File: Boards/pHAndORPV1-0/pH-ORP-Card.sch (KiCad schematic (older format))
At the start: 110 parts, among them IC1 PIC32MM0064GPM028, P1 ICSP, P2 AquaPicBus, P3 Power, P4 pH, P5 pH/ORP, Q1 NX7002AK, Q2 NX7002AK, Q3 NX7002AK, Q4 AO3407A, U1 AP2114H, U10 LTC2483, U11 Si8602, U12 TC7660, U2 ST485EC, U3 LMC6061, U4 TLV272, U5 LTC2483, U6 Si8602, U7 TC7660, U8 LMC6061, U9 TLV272, X1 8MHz

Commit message: worked on pH ORP board layout
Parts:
- P4, P5: footprint A_MyFootPrints:BNC_Socket_TYCO-AMP_LargePads -> MyFootPrints:BNC_Socket_TYCO-AMP_LargePads
- PS1, PS2: footprint A_MyFootPrints:8-SMD -> MyFootPrints:8-SMD
- RV1, RV2, RV3, RV4: footprint A_MyFootPrints:POTENTIAMETER_SMD -> MyFootPrints:POTENTIAMETER_SMD
- U10, U5: footprint A_MyFootPrints:DFN-10_3x3mm -> MyFootPrints:DFN-10_3x3mm
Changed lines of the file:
@@
 F 0 "P4" H 1660 1320 60  0000 C CNN
 F 1 "pH" V 1760 1140 40  0000 C CNN
-F 2 "A_MyFootPrints:BNC_Socket_TYCO-AMP_LargePads" H 1650 1200 60  0001 C CNN
+F 2 "MyFootPrints:BNC_Socket_TYCO-AMP_LargePads" H 1650 1200 60  0001 C CNN
 F 3 "~" H 1650 1200 60  0000 C CNN
 	1    1650 1200
@@
 F 0 "RV2" V 5150 2600 50  0000 C CNN
 F 1 "10K" V 5250 2600 50  0000 C CNN
-F 2 "A_MyFootPrints:POTENTIAMETER_SMD" H 5250 2600 60  0001 C CNN
+F 2 "MyFootPrints:POTENTIAMETER_SMD" H 5250 2600 60  0001 C CNN
 F 3 "~" H 5250 2600 60  0000 C CNN
 	1    5250 2600
@@
 F 0 "RV1" V 2850 2200 40  0000 C CNN
 F 1 "50K" V 2950 2200 40  0000 C CNN
-F 2 "A_MyFootPrints:POTENTIAMETER_SMD" H 2950 2200 60  0001 C CNN
+F 2 "MyFootPrints:POTENTIAMETER_SMD" H 2950 2200 60  0001 C CNN
 F 3 "~" H 2950 2200 60  0000 C CNN
 	1    2950 2200
@@
 F 0 "PS2" H 11250 4900 60  0000 C CNN
 F 1 "R1SE-0505" H 11450 4100 60  0000 C CNN
-F 2 "A_MyFootPrints:8-SMD" H 11450 4500 60  0001 C CNN
+F 2 "MyFootPrints:8-SMD" H 11450 4500 60  0001 C CNN
 F 3 "~" H 11450 4500 60  0000 C CNN
 	1    11450 4500
@@
 F 0 "PS1" H 11250 2000 60  0000 C CNN
 F 1 "R1SE-0505" H 11450 1200 60  0000 C CNN
-F 2 "A_MyFootPrints:8-SMD" H 11450 1600 60  0001 C CNN
+F 2 "MyFootPrints:8-SMD" H 11450 1600 60  0001 C CNN
 F 3 "~" H 11450 1600 60  0000 C CNN
 	1    11450 1600
@@
 F 0 "U5" H 7200 2500 60  0000 C CNN
 F 1 "LTC2483" H 7100 1900 60  0000 C CNN
-F 2 "A_MyFootPrints:DFN-10_3x3mm" H 7700 2200 60  0001 C CNN
+F 2 "MyFootPrints:DFN-10_3x3mm" H 7700 2200 60  0001 C CNN
 F 3 "~" H 7700 2200 60  0000 C CNN
 	1    7700 2200
@@
 F 0 "U10" H 7200 5400 60  0000 C CNN
 F 1 "LTC2483" H 7100 4800 60  0000 C CNN
-F 2 "A_MyFootPrints:DFN-10_3x3mm" H 7700 5100 60  0001 C CNN
+F 2 "MyFootPrints:DFN-10_3x3mm" H 7700 5100 60  0001 C CNN
 F 3 "~" H 7700 5100 60  0000 C CNN
 	1    7700 5100
@@
 F 0 "RV4" V 5150 5500 50  0000 C CNN
 F 1 "10K" V 5250 5500 50  0000 C CNN
-F 2 "A_MyFootPrints:POTENTIAMETER_SMD" H 5250 5500 60  0001 C CNN
+F 2 "MyFootPrints:POTENTIAMETER_SMD" H 5250 5500 60  0001 C CNN
 F 3 "~" H 5250 5500 60  0000 C CNN
 	1    5250 5500
@@
 F 0 "RV3" V 2850 5100 40  0000 C CNN
 F 1 "50K" V 2950 5100 40  0000 C CNN
-F 2 "A_MyFootPrints:POTENTIAMETER_SMD" H 2950 5100 60  0001 C CNN
+F 2 "MyFootPrints:POTENTIAMETER_SMD" H 2950 5100 60  0001 C CNN
 F 3 "~" H 2950 5100 60  0000 C CNN
 	1    2950 5100
@@
 F 0 "P5" H 1660 4220 60  0000 C CNN
 F 1 "pH/ORP" V 1760 4040 40  0000 C CNN
-F 2 "A_MyFootPrints:BNC_Socket_TYCO-AMP_LargePads" H 1650 4100 60  0001 C CNN
+F 2 "MyFootPrints:BNC_Socket_TYCO-AMP_LargePads" H 1650 4100 60  0001 C CNN
 F 3 "~" H 1650 4100 60  0000 C CNN
 	1    1650 4100

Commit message: added firmware for the pH ORP Card
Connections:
- net LED_R: now also IC1.3 (RB2); no longer IC1.1 (RB0)
- net LED_Y: now also IC1.1 (RB0); no longer IC1.3 (RB2)
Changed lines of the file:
@@
 RX_LV
 Text Label 2900 7400 2    60   ~ 0
-LED_Y
+LED_R
 Text Label 2900 7300 2    60   ~ 0
 LED_G
 Text Label 2900 7200 2    60   ~ 0
-LED_R
+LED_Y
 $Comp
 L TRI-LED D1

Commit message: something changed in schematic
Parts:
- D1: value SMP4-RGY -> SMTL4-RGY
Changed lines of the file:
@@
 P 3950 7250
 F 0 "D1" H 3950 7600 50  0000 C CNN
-F 1 "SMP4-RGY" H 3950 6860 50  0000 C CNN
+F 1 "SMTL4-RGY" H 3950 6860 50  0000 C CNN
 F 2 "MyFootPrints:PLCC-4" H 3950 7500 60  0001 C CNN
 F 3 "~" H 3950 7500 60  0000 C CNN

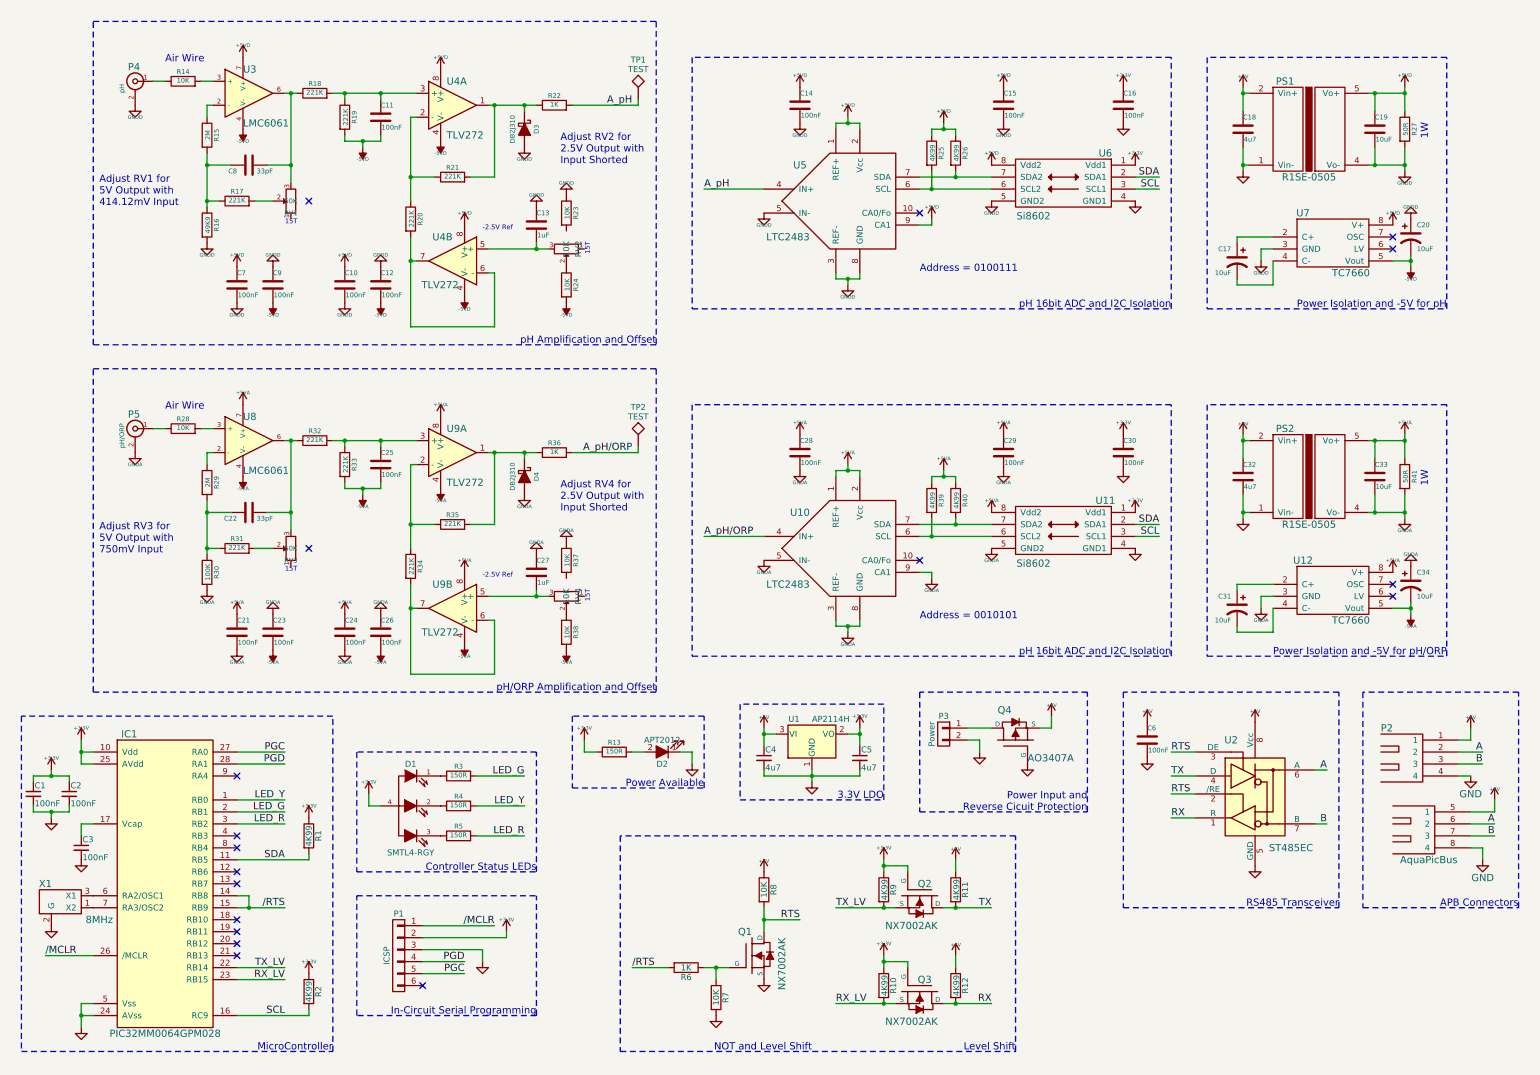
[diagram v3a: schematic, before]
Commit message: added enable disable for ph isolation
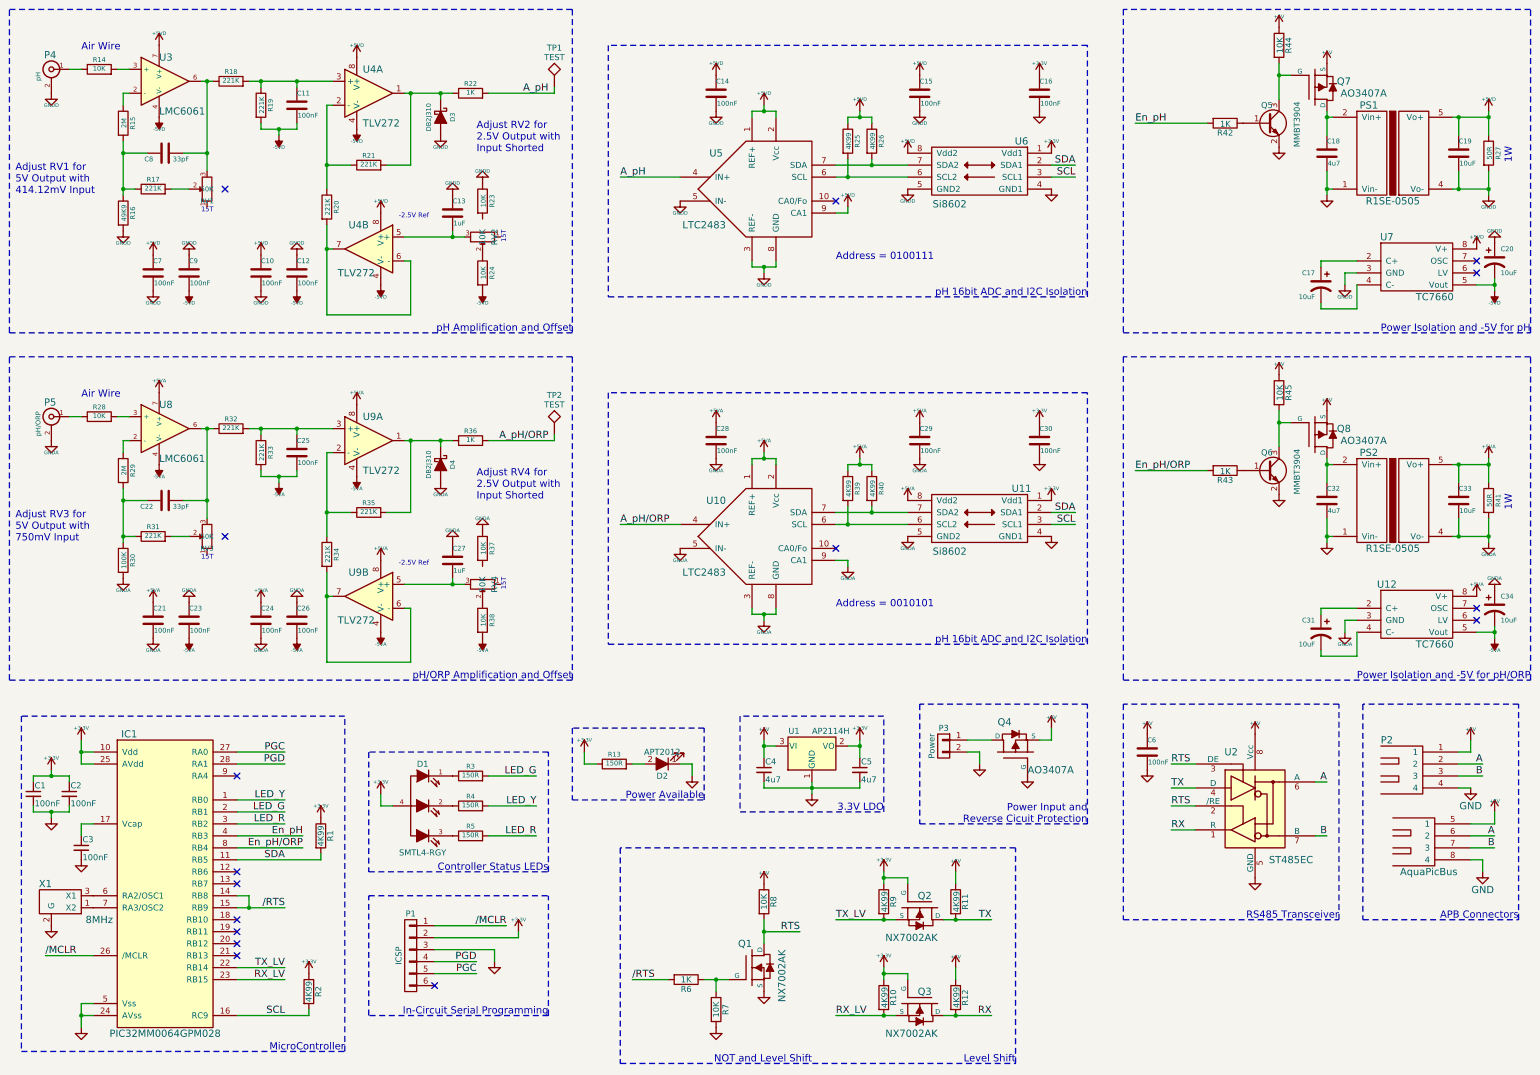
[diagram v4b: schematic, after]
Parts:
- added Q5, Q6: MMBT3904, TO_SOT_Packages_SMD:SOT-23, symbol Q_NPN_BEC
- added Q7, Q8: AO3407A, TO_SOT_Packages_SMD:SOT-23, symbol MOSFET_P_SMALL
- added R42, R43: 1K, Resistors_SMD:R_0805, symbol R
- added R44, R45: 10K, Resistors_SMD:R_0805, symbol R
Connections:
- net +5V: now also Q7.2 (S), Q8.2 (S), R44.1, R45.1; no longer C18.1, C32.1, PS1.2 (Vin+), PS2.2 (Vin+)
- net GND: now also Q5.2 (E), Q6.2 (E)
- net En_pH: now reaches IC1.4 (RB3)
- net En_pH: now also R42.2
- net En_pH/ORP: now reaches IC1.8 (RB4)
- net En_pH/ORP: now also R43.2
- new net: C18.1, PS1.2 (Vin+), Q7.3 (D)
- new net: C32.1, PS2.2 (Vin+), Q8.3 (D)
- new net: Q5.1 (B), R42.1
- new net: Q5.3 (C), Q7.1 (G), R44.2
- new net: Q6.1 (B), R43.1
- new net: Q6.3 (C), Q8.1 (G), R45.2
- no-connect marks 18 -> 16
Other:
- moved on the sheet: C10, C11, C12, C13, C14, C15, C16, C17, C18, C19, C20, C21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

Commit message: kicad updating something
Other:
- moved on the sheet: P2

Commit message: refactored Digital Input to PIC32
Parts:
- P1: value ICSP -> 1x6 2.54 Pin Header
- P3: value Power -> 1x2 2.54
- P4: value pH -> BNC
- P5: value pH/ORP -> BNC
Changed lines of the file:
@@
 P 950 1100
 F 0 "P4" H 960 1220 60  0000 C CNN
-F 1 "pH" V 1060 1040 40  0000 C CNN
+F 1 "BNC" V 1060 1040 40  0001 C CNN
 F 2 "MyFootPrints:BNC_Socket_TYCO-AMP_LargePads" H 950 1100 60  0001 C CNN
 F 3 "~" H 950 1100 60  0000 C CNN
@@
 P 3950 8500
 F 0 "P1" H 3950 8850 50  0000 C CNN
-F 1 "ICSP" V 4050 8500 50  0000 C CNN
+F 1 "1x6 2.54 Pin Header" V 4050 8500 50  0001 C CNN
 F 2 "Pin_Headers:Pin_Header_Straight_1x06_Pitch2.54mm" H 3950 8500 60  0001 C CNN
 F 3 "" H 3950 8500 60  0000 C CNN
@@
 P 8400 6750
 F 0 "P3" H 8400 6900 50  0000 C CNN
-F 1 "Power" V 8500 6750 50  0000 C CNN
+F 1 "1x2 2.54" V 8500 6750 50  0001 C CNN
 F 2 "MyFootPrints:Screw_Header_1x2" H 8400 6750 60  0001 C CNN
 F 3 "" H 8400 6750 60  0000 C CNN
@@
 P 950 4000
 F 0 "P5" H 960 4120 60  0000 C CNN
-F 1 "pH/ORP" V 1060 3940 40  0000 C CNN
+F 1 "BNC" V 1060 3940 40  0001 C CNN
 F 2 "MyFootPrints:BNC_Socket_TYCO-AMP_LargePads" H 950 4000 60  0001 C CNN
 F 3 "~" H 950 4000 60  0000 C CNN

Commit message: must have made changes to some schematics
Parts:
- TP1, TP2: symbol TEST -> TEST_1P
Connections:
- net at C8.2, R18.1, U3.6: now also RV1.2; no longer RV1.3
- net at R17.2: now also RV1.1; no longer RV1.2
- net at C13.2, U4.5 (+): now also RV2.2; no longer RV2.3
- net at RV2.1: now also R24.1
- net at R23.2: now also RV2.3
- net at C22.2, R32.1, U8.6: now also RV3.2; no longer RV3.3
- net at R31.2: now also RV3.1; no longer RV3.2
- net at C27.2, U9.5 (+): now also RV4.2; no longer RV4.3
- net at RV4.1: now also R38.1
- net at R37.2: now also RV4.3
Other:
- moved on the sheet: RV1, RV2, RV3, RV4, TP1, TP2
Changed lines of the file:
@@
 U 1 1 5395A144
 P 4550 2500
-F 0 "RV2" V 4450 2500 50  0000 C CNN
-F 1 "10K" V 4550 2500 50  0000 C CNN
+F 0 "RV2" H 4550 2400 50  0000 C CNN
+F 1 "10K" H 4550 2500 50  0000 C CNN
 F 2 "MyFootPrints:POTENTIAMETER_SMD" H 4550 2500 60  0001 C CNN
 F 3 "~" H 4550 2500 60  0000 C CNN
 	1    4550 2500
-	-1   0    0    1
+	0    -1   -1   0
 $EndComp
 $Comp
@@
 U 1 1 5395AF86
 P 2250 2100
-F 0 "RV1" V 2150 2100 40  0000 C CNN
-F 1 "50K" V 2250 2100 40  0000 C CNN
+F 0 "RV1" H 2250 2000 40  0000 C CNN
+F 1 "50K" H 2250 2100 40  0000 C CNN
 F 2 "MyFootPrints:POTENTIAMETER_SMD" H 2250 2100 60  0001 C CNN
 F 3 "~" H 2250 2100 60  0000 C CNN
 	1    2250 2100
-	0    -1   -1   0
+	1    0    0    -1
 $EndComp
 NoConn ~ 2400 2100
@@
 $EndComp
 $Comp
-L TEST TP1
+L TEST_1P TP1
 U 1 1 5A296A71
 P 5150 1250
@@
 U 1 1 5A298BB5
 P 4550 5400
-F 0 "RV4" V 4450 5400 50  0000 C CNN
-F 1 "10K" V 4550 5400 50  0000 C CNN
+F 0 "RV4" H 4550 5300 50  0000 C CNN
+F 1 "10K" H 4550 5400 50  0000 C CNN
 F 2 "MyFootPrints:POTENTIAMETER_SMD" H 4550 5400 60  0001 C CNN
 F 3 "~" H 4550 5400 60  0000 C CNN
 	1    4550 5400
-	-1   0    0    1
+	0    -1   -1   0
 $EndComp
 $Comp
@@
 U 1 1 5A298BCE
 P 2250 5000
-F 0 "RV3" V 2150 5000 40  0000 C CNN
-F 1 "50K" V 2250 5000 40  0000 C CNN
+F 0 "RV3" H 2250 4900 40  0000 C CNN
+F 1 "50K" H 2250 5000 40  0000 C CNN
 F 2 "MyFootPrints:POTENTIAMETER_SMD" H 2250 5000 60  0001 C CNN
 F 3 "~" H 2250 5000 60  0000 C CNN
 	1    2250 5000
-	0    -1   -1   0
+	1    0    0    -1
 $EndComp
 NoConn ~ 2400 5000
@@
 Connection ~ 1550 5000
 $Comp
-L TEST TP2
+L TEST_1P TP2
 U 1 1 5A298C96
 P 5150 4150

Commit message: upgrade pH ORP to KiCAD 5
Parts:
- C1, C2, C3, C4, C5: symbol C_Small -> pH-ORP-Card-rescue:C_Small
- C10, C11, C12, C13, C14, C15, C16, C18, C19, C21, C22, C23, C24, C25, C26, C27, C28, C29, C30, C32, C33, C6, C7, C8, C9: symbol C -> pH-ORP-Card-rescue:C
- C17, C20, C31, C34: symbol CP1 -> pH-ORP-Card-rescue:CP1
- D1: symbol TRI-LED -> GoodtimeDev:TRI-LED
- D2: symbol LED_ALT -> pH-ORP-Card-rescue:LED_ALT
- D3, D4: symbol D_Schottky_ALT -> pH-ORP-Card-rescue:D_Schottky_ALT
- IC1: symbol PIC32MM0064GPM028_QFN -> GoodtimeDev:PIC32MM0064GPM028_QFN
- P1: symbol CONN_01X06 -> pH-ORP-Card-rescue:CONN_01X06
- P2: symbol USB1.0_Stacked -> GoodtimeDev:USB1.0_Stacked
- P3: symbol CONN_01X02 -> pH-ORP-Card-rescue:CONN_01X02
- P4, P5: symbol BNC -> pH-ORP-Card-rescue:BNC
- PS1, PS2: symbol ROE-0505S -> GoodtimeDev:ROE-0505S
- Q1, Q2, Q3: symbol MOSFET_N_SMALL -> GoodtimeDev:MOSFET_N_SMALL
- Q4, Q7, Q8: symbol MOSFET_P_SMALL -> GoodtimeDev:MOSFET_P_SMALL
- Q5, Q6: symbol Q_NPN_BEC -> pH-ORP-Card-rescue:Q_NPN_BEC
- R1, R10, R11, R12, R13, R14, R15, R16, R17, R18, R19, R2, R20, R21, R22, R23, R24, R25, R26, R27, R28, R29, R3, R30, R31, R32, R33, R34, R35, R36, R37, R38, R39, R4, R40, R41, R42, R43, R44, R45, R5, R6, R7, R8, R9: symbol R -> pH-ORP-Card-rescue:R
- RV1, RV2, RV3, RV4: symbol POT -> pH-ORP-Card-rescue:POT
- TP1, TP2: symbol TEST_1P -> pH-ORP-Card-rescue:TEST_1P
- U1: symbol AP1117-33 -> pH-ORP-Card-rescue:AP1117-33
- U10, U5: symbol LTC2483 -> GoodtimeDev:LTC2483
- U11, U6: symbol Si8602 -> GoodtimeDev:Si8602
- U12, U7: symbol TC7660 -> GoodtimeDev:TC7660
- U2: symbol SN75176B -> GoodtimeDev:SN75176B
- U3, U8: symbol LMC6061 -> GoodtimeDev:LMC6061
- U4, U9: symbol LM358 -> pH-ORP-Card-rescue:LM358
- X1: symbol RESONATOR -> GoodtimeDev:RESONATOR
